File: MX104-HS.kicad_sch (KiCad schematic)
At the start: 57 parts, among them J1 Conn_01x03, SW1 Reset, SW2 Boot, U1 RP2040, U2 IS31FL3742A-QFLS4-TR, U3 W25Q128JVS, U4 IS31FL3742A-QFLS4-TR, U5 NCP1117-3.3_SOT223, Y1 ABLS-12.000MHZ-B4-T

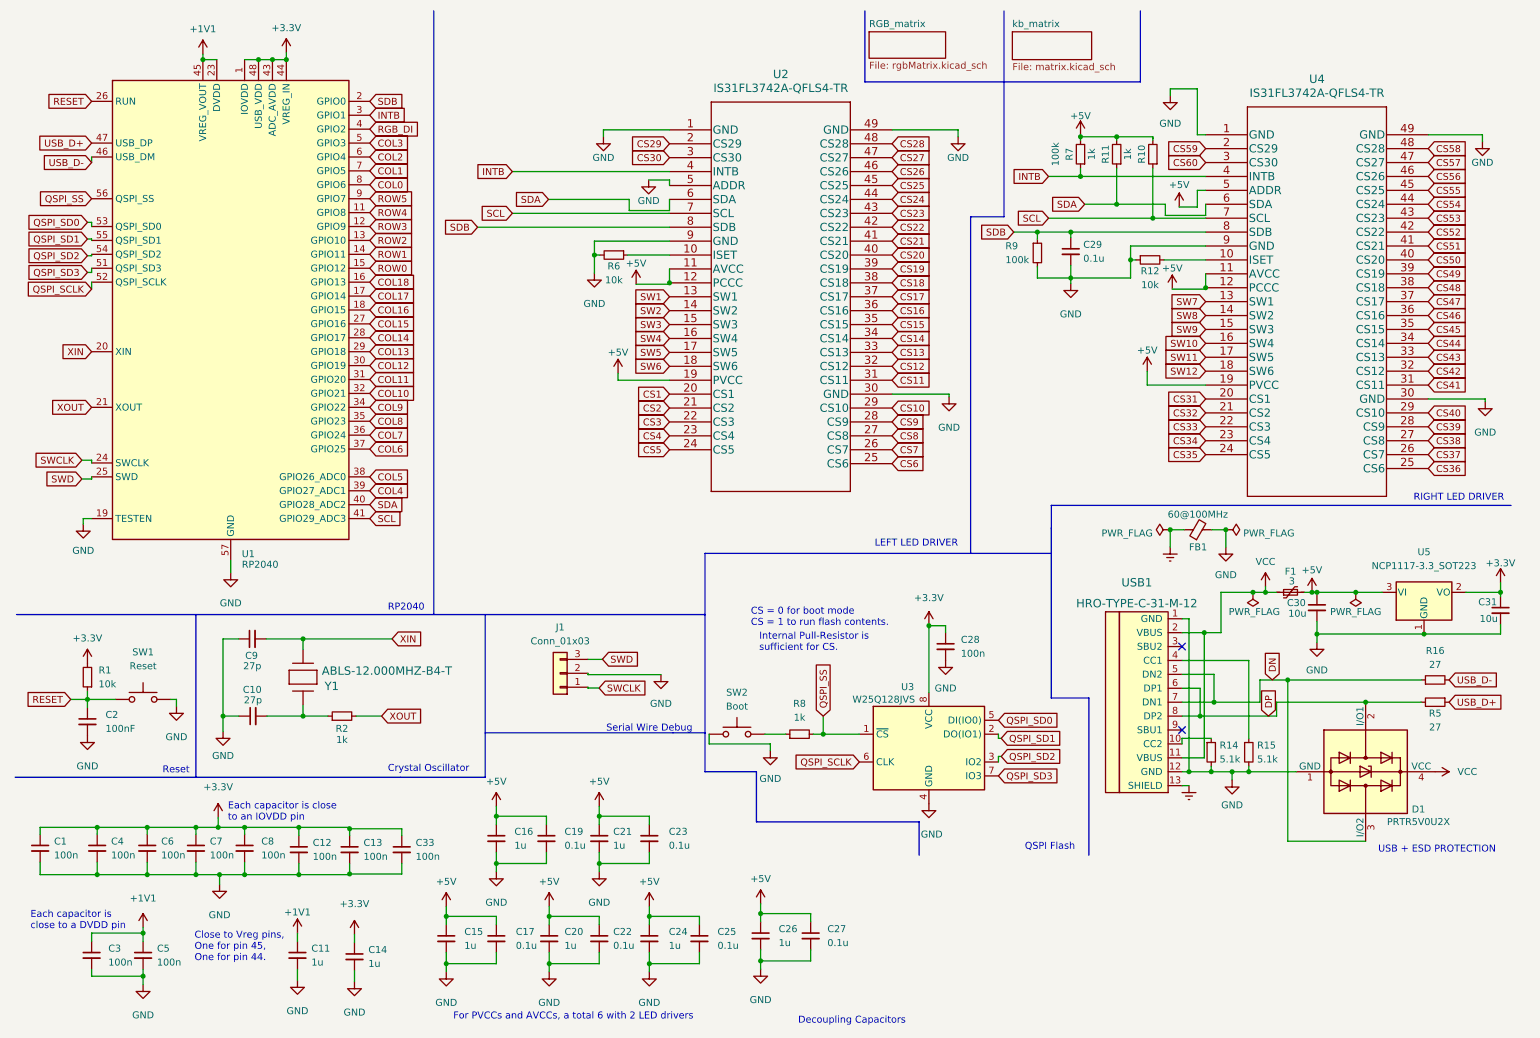
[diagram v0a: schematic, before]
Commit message: Began changing out backlight for better components
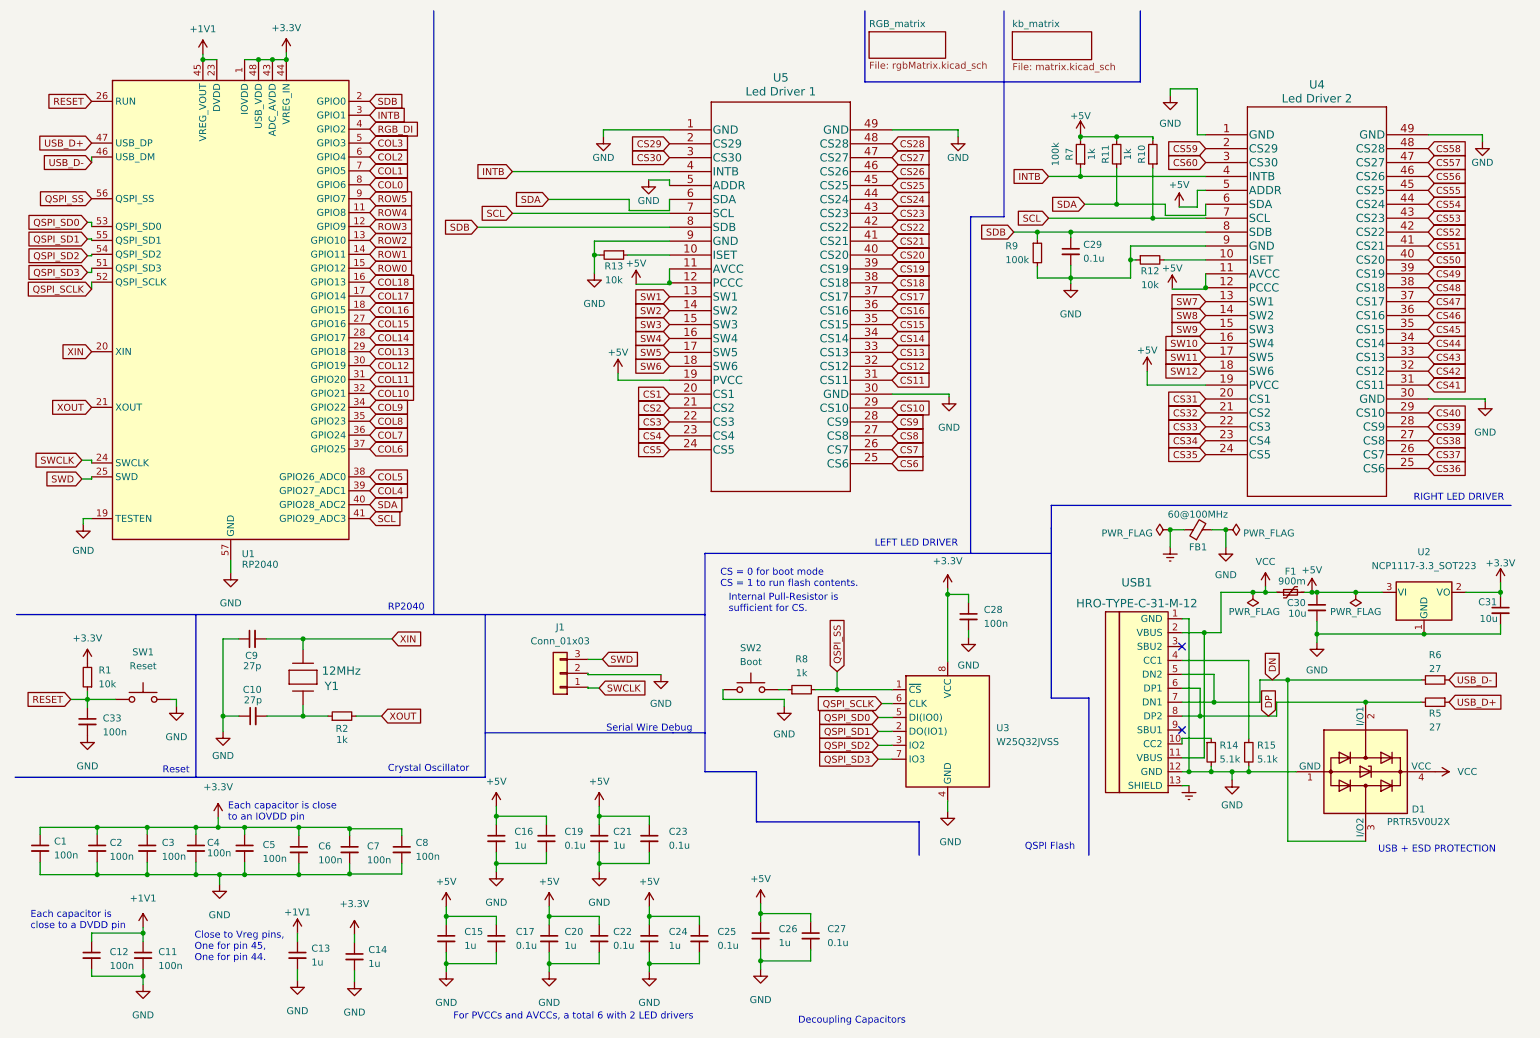
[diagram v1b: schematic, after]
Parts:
- removed U3: W25Q128JVS, Package_SO:SOIC-8_5.23x5.23mm_P1.27mm, symbol Memory_Flash:W25Q128JVS
- added U3: W25Q32JVSS, Package_SO:SOIC-8_5.23x5.23mm_P1.27mm, symbol Memory_Flash:W25Q32JVSS
- C33: renamed from C2; value 100nF -> 100n
- F1: value 3 -> 900m
- FB1: footprint Inductor_SMD:L_0805_2012Metric_Pad1.15x1.40mm_HandSolder -> Inductor_SMD:L_1206_3216Metric_Pad1.42x1.75mm_HandSolder
- U4: value IS31FL3742A-QFLS4-TR -> Led Driver 2
- U5: renamed from U2; value IS31FL3742A-QFLS4-TR -> Led Driver 1
- Y1: value ABLS-12.000MHZ-B4-T -> 12MHz
- renumbered C5 to C11, C3 to C12, C11 to C13, C4 to C2, C6 to C3, C7 to C4, C8 to C5, C12 to C6, C13 to C7, C33 to C8, R6 to R13, R16 to R6, U5 to U2
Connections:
- net +3.3V: now also U3.8 (VCC)
- net GND: now also U3.4 (GND)
- net QSPI_SCLK: now also U3.6 (CLK)
- net QSPI_SD0: now also U3.5 (DI(IO0))
- net QSPI_SD1: now also U3.2 (DO(IO1))
- net QSPI_SD2: now also U3.3 (IO2)
- net QSPI_SD3: now also U3.7 (IO3)
- net QSPI_SS: now also U3.1 (~{CS})
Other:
- moved on the sheet: C28, R8, SW2

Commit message: Finished version 1.0
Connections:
- net COL0: now also U1.41 (GPIO29_ADC3); no longer U1.8 (GPIO6)
- net COL1: now also U1.40 (GPIO28_ADC2); no longer U1.7 (GPIO5)
- net COL10: now also U1.30 (GPIO19); no longer U1.32 (GPIO21)
- net COL11: now also U1.29 (GPIO18); no longer U1.31 (GPIO20)
- net COL12: now also U1.28 (GPIO17); no longer U1.30 (GPIO19)
- net COL13: now also U1.27 (GPIO16); no longer U1.29 (GPIO18)
- net COL14: now also U1.17 (GPIO14); no longer U1.28 (GPIO17)
- net COL15: now also U1.16 (GPIO13); no longer U1.27 (GPIO16)
- net COL16: now also U1.11 (GPIO8); no longer U1.18 (GPIO15)
- net COL17: now also U1.9 (GPIO7); no longer U1.17 (GPIO14)
- net COL18: now also U1.8 (GPIO6); no longer U1.16 (GPIO13)
- net COL2: now also U1.39 (GPIO27_ADC1); no longer U1.6 (GPIO4)
- net COL3: now also U1.38 (GPIO26_ADC0); no longer U1.5 (GPIO3)
- net COL4: now also U1.37 (GPIO25); no longer U1.39 (GPIO27_ADC1)
- net COL5: now also U1.36 (GPIO24); no longer U1.38 (GPIO26_ADC0)
- net COL6: now also U1.35 (GPIO23); no longer U1.37 (GPIO25)
- net COL7: now also U1.34 (GPIO22); no longer U1.36 (GPIO24)
- net COL8: now also U1.32 (GPIO21); no longer U1.35 (GPIO23)
- net COL9: now also U1.31 (GPIO20); no longer U1.34 (GPIO22)
- net INTB: now also U1.15 (GPIO12); no longer U1.3 (GPIO1)
- net RGB_DI: now also U1.18 (GPIO15); no longer U1.4 (GPIO2)
- net ROW0: now also U1.7 (GPIO5); no longer U1.15 (GPIO12)
- net ROW1: now also U1.6 (GPIO4); no longer U1.14 (GPIO11)
- net ROW2: now also U1.5 (GPIO3); no longer U1.13 (GPIO10)
- net ROW3: now also U1.4 (GPIO2); no longer U1.12 (GPIO9)
- net ROW4: now also U1.3 (GPIO1); no longer U1.11 (GPIO8)
- net ROW5: now also U1.2 (GPIO0); no longer U1.9 (GPIO7)
- net SCL: now also U1.13 (GPIO10); no longer U1.41 (GPIO29_ADC3)
- net SDA: now also U1.14 (GPIO11); no longer U1.40 (GPIO28_ADC2)
- net SDB: now also U1.12 (GPIO9); no longer U1.2 (GPIO0)
